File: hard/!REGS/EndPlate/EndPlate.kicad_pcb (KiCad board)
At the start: 2 copper layers, 68.6 x 61 mm, 10 parts, among them J1 Conn_01x13_Socket, J2 Conn_01x13_Socket, J3 Conn_01x13_Socket, J4 Conn_01x13_Socket, J5 Conn_01x13_Socket, J6 Conn_01x13_Socket, J7 Conn_01x13_Socket, J8 Conn_01x13_Socket, U1 74HC245, U2 74HC245

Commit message: End Plate PCB in work
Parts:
- added J10: Conn_01x03_Pin, Connector_PinHeader_2.54mm:PinHeader_1x03_P2.54mm_Vertical, F.Cu at (109.2, 43.2)
- added J9: Conn_01x03_Pin, Connector_PinHeader_2.54mm:PinHeader_1x03_P2.54mm_Vertical, F.Cu at (109.2, 53.3)
- J1, J2, J3, J4, J5, J6, J7, J8: footprint Connector_PinSocket_2.54mm:PinSocket_1x13_P2.54mm_Vertical -> Connector_PinSocket_2.54mm:PinSocket_1x13_P2.54mm_Vertical_SMD_Pin1Left
- moved J8 55.4 mm to (50.8, 40.6), turned to 180 degrees
- moved J1 55.4 mm to (104.1, 40.6), turned to 180 degrees
- moved J2 41.0 mm to (96.5, 40.6), turned to 180 degrees
- moved J7 41.0 mm to (58.4, 40.6), turned to 180 degrees
- moved J3 27.4 mm to (88.9, 40.6), turned to 180 degrees
- moved J6 27.4 mm to (66.0, 40.6), turned to 180 degrees
- moved U1 23.4 mm to (73.7, 68.6), turned to -90 degrees
- moved U2 23.4 mm to (104.1, 68.6), turned to -90 degrees
- moved J4 16.8 mm to (81.3, 40.6), turned to 180 degrees
- moved J5 16.8 mm to (73.7, 40.6), turned to 180 degrees
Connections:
- J1 pad 10: /S1.2 -> unconnected-(J1-Pin_10-Pad10)
- J1 pad 11: /~E1 -> /DST0
- J1 pad 6: /DST0 -> /S1.0
- J1 pad 7: unconnected-(J1-Pin_7-Pad7) -> /S1.1
- J1 pad 8: /S1.0 -> /S1.2
- J1 pad 9: /S1.1 -> /~E1
- J2 pad 10: /S1.2 -> unconnected-(J2-Pin_10-Pad10)
- J2 pad 11: /~E1 -> /DST1
- J2 pad 6: /DST1 -> /S1.0
- J2 pad 7: unconnected-(J2-Pin_7-Pad7) -> /S1.1
- J2 pad 8: /S1.0 -> /S1.2
- J2 pad 9: /S1.1 -> /~E1
- J3 pad 10: /S1.2 -> unconnected-(J3-Pin_10-Pad10)
- J3 pad 11: /~E1 -> /DST2
- J3 pad 6: /DST2 -> /S1.0
- J3 pad 7: unconnected-(J3-Pin_7-Pad7) -> /S1.1
- J3 pad 8: /S1.0 -> /S1.2
- J3 pad 9: /S1.1 -> /~E1
- J4 pad 10: /S1.2 -> unconnected-(J4-Pin_10-Pad10)
- J4 pad 11: /~E1 -> /DST3
- J4 pad 6: /DST3 -> /S1.0
- J4 pad 7: unconnected-(J4-Pin_7-Pad7) -> /S1.1
- J4 pad 8: /S1.0 -> /S1.2
- J4 pad 9: /S1.1 -> /~E1
- J5 pad 10: /S1.2 -> unconnected-(J5-Pin_10-Pad10)
- J5 pad 11: /~E1 -> /DST4
- J5 pad 6: /DST4 -> /S1.0
- J5 pad 7: unconnected-(J5-Pin_7-Pad7) -> /S1.1
- J5 pad 8: /S1.0 -> /S1.2
- J5 pad 9: /S1.1 -> /~E1
- J6 pad 10: /S1.2 -> unconnected-(J6-Pin_10-Pad10)
- J6 pad 11: /~E1 -> /DST5
- J6 pad 6: /DST5 -> /S1.0
- J6 pad 7: unconnected-(J6-Pin_7-Pad7) -> /S1.1
- J6 pad 8: /S1.0 -> /S1.2
- J6 pad 9: /S1.1 -> /~E1
- J7 pad 10: /S1.2 -> unconnected-(J7-Pin_10-Pad10)
- J7 pad 11: /~E1 -> /DST6
- J7 pad 6: /DST6 -> /S1.0
- J7 pad 7: unconnected-(J7-Pin_7-Pad7) -> /S1.1
- J7 pad 8: /S1.0 -> /S1.2
- J7 pad 9: /S1.1 -> /~E1
- J8 pad 10: /S1.2 -> unconnected-(J8-Pin_10-Pad10)
- J8 pad 11: /~E1 -> /DST7
- J8 pad 6: /DST7 -> /S1.0
- J8 pad 7: unconnected-(J8-Pin_7-Pad7) -> /S1.1
- J8 pad 8: /S1.0 -> /S1.2
- J8 pad 9: /S1.1 -> /~E1
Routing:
- net /S1.2: track 0.00 -> 60.1 mm
- net /S1.0: track 0.00 -> 60.1 mm
- net /S0.2: track 0.00 -> 60.1 mm
- net /S0.0: track 0.00 -> 60.1 mm
- net /S1.1: track 0.00 -> 56.8 mm
- net /S0.1: track 0.00 -> 56.8 mm
- net VCC: track 0.00 -> 53.3 mm
- net GND: track 0.00 -> 53.3 mm
- net /~E1: track 0.00 -> 53.3 mm
- net /~E0: track 0.00 -> 53.3 mm
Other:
- board text added: "The connectors are installed upside down because the multiplexer boards are installed upside down!"

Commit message: End Plate in work
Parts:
- added C1: 0,1uF, Capacitor_THT:C_Axial_L12.0mm_D6.5mm_P15.00mm_Horizontal, B.Cu at (82.5, 71.1)
- added C2: 0,1uF, Capacitor_THT:C_Axial_L12.0mm_D6.5mm_P15.00mm_Horizontal, B.Cu at (102.9, 71.2)
- added J11: Conn_01x09_Pin, Connector_PinHeader_2.54mm:PinHeader_1x09_P2.54mm_Vertical, F.Cu at (90.2, 67.3)
- added J12: Conn_01x09_Pin, Connector_PinHeader_2.54mm:PinHeader_1x09_P2.54mm_Vertical, F.Cu at (110.5, 67.3)
- added J13: Conn_01x09_Pin, Connector_PinHeader_2.54mm:PinHeader_1x09_P2.54mm_Vertical, F.Cu at (113.0, 67.3)
- added J14: Conn_01x09_Pin, Connector_PinHeader_2.54mm:PinHeader_1x09_P2.54mm_Vertical, F.Cu at (92.7, 67.3)
- added J15: Conn_01x01_Pin, Connector_PinHeader_2.54mm:PinHeader_1x01_P2.54mm_Vertical, F.Cu at (90.8, 61.6)
- added J16: Conn_01x01_Pin, Connector_PinHeader_2.54mm:PinHeader_1x01_P2.54mm_Vertical, F.Cu at (111.1, 61.6)
- added R1: 10k, Resistor_SMD:R_0805_2012Metric_Pad1.20x1.40mm_HandSolder, B.Cu at (82.5, 64.8)
- added R2: 10k, Resistor_SMD:R_0805_2012Metric_Pad1.20x1.40mm_HandSolder, B.Cu at (102.9, 64.8)
- added R3: 10k, Resistor_SMD:R_0805_2012Metric_Pad1.20x1.40mm_HandSolder, B.Cu at (91.7, 64.8)
- added R4: 10k, Resistor_SMD:R_0805_2012Metric_Pad1.20x1.40mm_HandSolder, B.Cu at (112.0, 64.8)
- J1, J2, J3, J4, J5, J6, J7, J8: moved to B.Cu
- moved J9 7.85 mm to (111.1, 45.7)
- moved J10 7.85 mm to (111.1, 35.6)
- moved U1 6.35 mm to (78.7, 64.8), turned to 0 degrees
- moved U2 6.35 mm to (99.1, 64.8), turned to 0 degrees
- turned J1 to 0 degrees
- turned J2 to 0 degrees
- turned J3 to 0 degrees
- turned J4 to 0 degrees
- turned J5 to 0 degrees
- turned J6 to 0 degrees
- turned J7 to 0 degrees
- turned J8 to 0 degrees
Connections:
- J1 pad 1: VCC -> /DST0
- J1 pad 10: unconnected-(J1-Pin_10-Pad10) -> /S1.1
- J1 pad 11: /DST0 -> /S1.2
- J1 pad 12: /SRC0 -> /~E1
- J1 pad 2: /S0.0 -> /SRC0
- J1 pad 3: /S0.1 -> unconnected-(J1-Pin_3-Pad3)
- J1 pad 4: /S0.2 -> VCC
- J1 pad 5: /~E0 -> /S0.0
- J1 pad 6: /S1.0 -> /S0.1
- J1 pad 7: /S1.1 -> /S0.2
- J1 pad 8: /S1.2 -> /~E0
- J1 pad 9: /~E1 -> /S1.0
- J2 pad 1: VCC -> /DST1
- J2 pad 10: unconnected-(J2-Pin_10-Pad10) -> /S1.1
- J2 pad 11: /DST1 -> /S1.2
- J2 pad 12: /SRC1 -> /~E1
- J2 pad 2: /S0.0 -> /SRC1
- J2 pad 3: /S0.1 -> unconnected-(J2-Pin_3-Pad3)
- J2 pad 4: /S0.2 -> VCC
- J2 pad 5: /~E0 -> /S0.0
- J2 pad 6: /S1.0 -> /S0.1
- J2 pad 7: /S1.1 -> /S0.2
- J2 pad 8: /S1.2 -> /~E0
- J2 pad 9: /~E1 -> /S1.0
- J3 pad 1: VCC -> /DST2
- J3 pad 10: unconnected-(J3-Pin_10-Pad10) -> /S1.1
- J3 pad 11: /DST2 -> /S1.2
- J3 pad 12: /SRC2 -> /~E1
- J3 pad 2: /S0.0 -> /SRC2
- J3 pad 3: /S0.1 -> unconnected-(J3-Pin_3-Pad3)
- J3 pad 4: /S0.2 -> VCC
- J3 pad 5: /~E0 -> /S0.0
- J3 pad 6: /S1.0 -> /S0.1
- J3 pad 7: /S1.1 -> /S0.2
- J3 pad 8: /S1.2 -> /~E0
- J3 pad 9: /~E1 -> /S1.0
- J4 pad 1: VCC -> /DST3
- J4 pad 10: unconnected-(J4-Pin_10-Pad10) -> /S1.1
- J4 pad 11: /DST3 -> /S1.2
- J4 pad 12: /SRC3 -> /~E1
- J4 pad 2: /S0.0 -> /SRC3
- J4 pad 3: /S0.1 -> unconnected-(J4-Pin_3-Pad3)
- J4 pad 4: /S0.2 -> VCC
- J4 pad 5: /~E0 -> /S0.0
- J4 pad 6: /S1.0 -> /S0.1
- J4 pad 7: /S1.1 -> /S0.2
- J4 pad 8: /S1.2 -> /~E0
- J4 pad 9: /~E1 -> /S1.0
- J5 pad 1: VCC -> /DST4
- J5 pad 10: unconnected-(J5-Pin_10-Pad10) -> /S1.1
- J5 pad 11: /DST4 -> /S1.2
- J5 pad 12: /SRC4 -> /~E1
- J5 pad 2: /S0.0 -> /SRC4
- J5 pad 3: /S0.1 -> unconnected-(J5-Pin_3-Pad3)
- J5 pad 4: /S0.2 -> VCC
- J5 pad 5: /~E0 -> /S0.0
- J5 pad 6: /S1.0 -> /S0.1
- J5 pad 7: /S1.1 -> /S0.2
- J5 pad 8: /S1.2 -> /~E0
- J5 pad 9: /~E1 -> /S1.0
- J6 pad 1: VCC -> /DST5
- J6 pad 10: unconnected-(J6-Pin_10-Pad10) -> /S1.1
- J6 pad 11: /DST5 -> /S1.2
- J6 pad 12: /SRC5 -> /~E1
- J6 pad 2: /S0.0 -> /SRC5
- J6 pad 3: /S0.1 -> unconnected-(J6-Pin_3-Pad3)
- J6 pad 4: /S0.2 -> VCC
- J6 pad 5: /~E0 -> /S0.0
- J6 pad 6: /S1.0 -> /S0.1
- J6 pad 7: /S1.1 -> /S0.2
- J6 pad 8: /S1.2 -> /~E0
- J6 pad 9: /~E1 -> /S1.0
- J7 pad 1: VCC -> /DST6
- J7 pad 10: unconnected-(J7-Pin_10-Pad10) -> /S1.1
- J7 pad 11: /DST6 -> /S1.2
- J7 pad 12: /SRC6 -> /~E1
- J7 pad 2: /S0.0 -> /SRC6
- J7 pad 3: /S0.1 -> unconnected-(J7-Pin_3-Pad3)
- J7 pad 4: /S0.2 -> VCC
- J7 pad 5: /~E0 -> /S0.0
- J7 pad 6: /S1.0 -> /S0.1
- J7 pad 7: /S1.1 -> /S0.2
- J7 pad 8: /S1.2 -> /~E0
- J7 pad 9: /~E1 -> /S1.0
- J8 pad 1: VCC -> /DST7
- J8 pad 10: unconnected-(J8-Pin_10-Pad10) -> /S1.1
- J8 pad 11: /DST7 -> /S1.2
- J8 pad 12: /SRC7 -> /~E1
- J8 pad 2: /S0.0 -> /SRC7
- J8 pad 3: /S0.1 -> unconnected-(J8-Pin_3-Pad3)
- J8 pad 4: /S0.2 -> VCC
- J8 pad 5: /~E0 -> /S0.0
- J8 pad 6: /S1.0 -> /S0.1
- J8 pad 7: /S1.1 -> /S0.2
- J8 pad 8: /S1.2 -> /~E0
- J8 pad 9: /~E1 -> /S1.0
- U1 pad 1: unconnected-(U1-A->B-Pad1) -> Net-(U1-A->B)
- U1 pad 19: unconnected-(U1-CE-Pad19) -> Net-(J15-Pin_1)
- U2 pad 1: unconnected-(U2-A->B-Pad1) -> Net-(U2-A->B)
- U2 pad 19: unconnected-(U2-CE-Pad19) -> Net-(J16-Pin_1)
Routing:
- net GND: track 53.3 -> 261.4 mm
- net /SRC7: track 0.00 -> 76.0 mm
- net /SRC6: track 0.00 -> 66.6 mm
- net /DST7: track 0.00 -> 57.7 mm
- net /SRC5: track 0.00 -> 56.4 mm
- net /SRC3: track 0.00 -> 53.6 mm
- net /SRC4: track 0.00 -> 53.2 mm
- net /DST6: track 0.00 -> 48.3 mm
- net /SRC2: track 0.00 -> 44.5 mm
- net VCC: track 53.3 -> 94.3 mm
- net /DST5: track 0.00 -> 38.5 mm
- net /DST0: track 0.00 -> 35.7 mm
- net /DST1: track 0.00 -> 33.6 mm
- net /DST4: track 0.00 -> 32.2 mm
- net /DST3: track 0.00 -> 31.3 mm
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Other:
- board size 68.6 x 61 mm -> 74.9 x 68.6 mm
- board text added: "DST"
- board text added: "Gnd"
- board text added: "SRC"

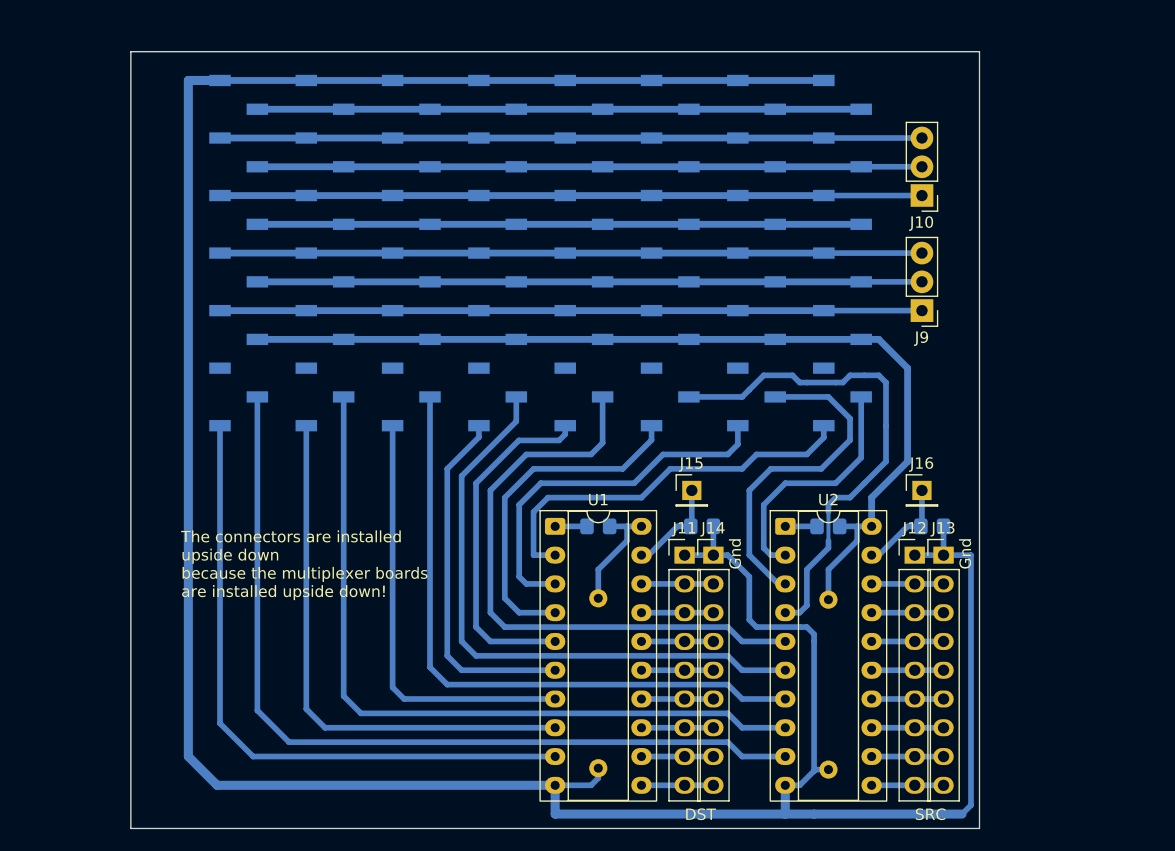
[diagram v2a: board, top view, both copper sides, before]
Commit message: End Plate polishing
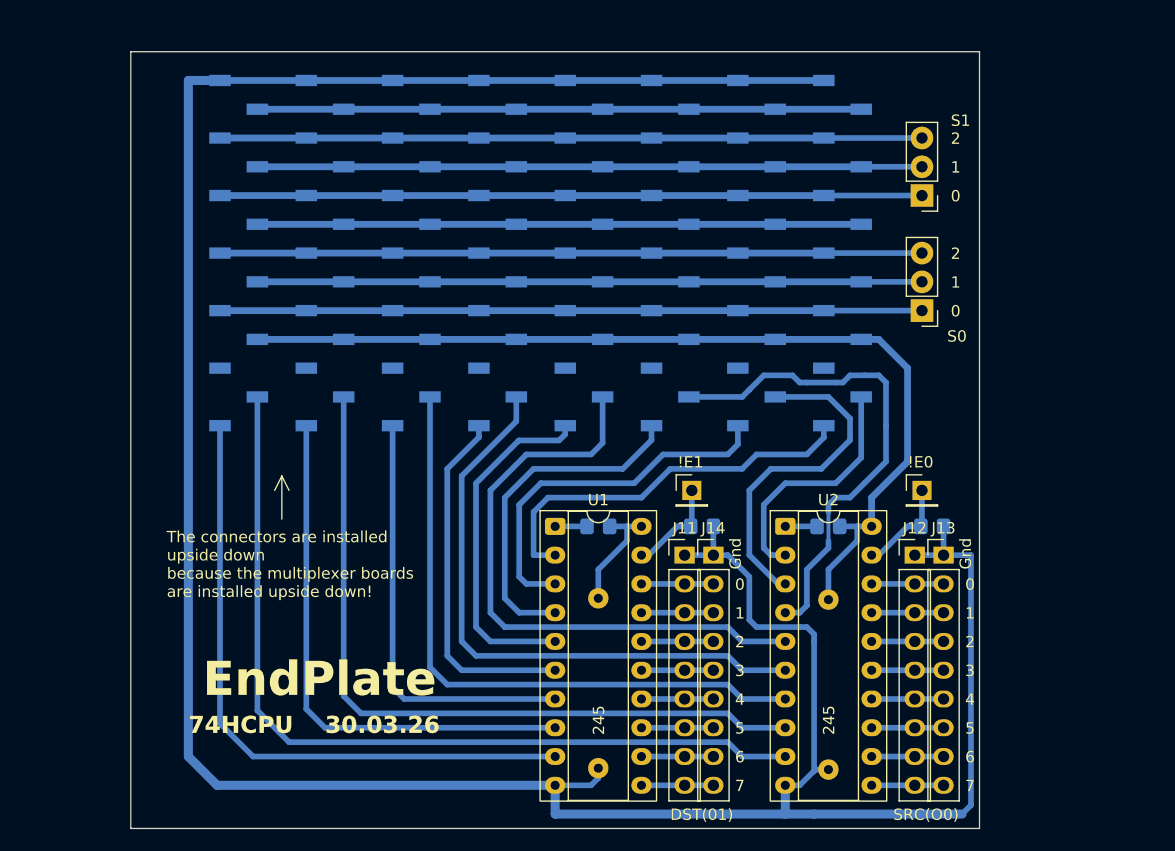
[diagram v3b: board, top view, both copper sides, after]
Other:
- board text added: "!E0"
- board text added: "!E1"
- board text added: "0"
- board text added: "1"
- board text added: "2"
- board text added: "245"
- board text added: "3"
- board text added: "30.03.26"
- board text added: "4"
- board text added: "5"
- board text added: "6"
- board text added: "7"
- board text added: "74HCPU"
- board text added: "DST(01)"
- board text added: "EndPlate"
- board text added: "S0"
- board text added: "S1"
- board text added: "SRC(O0)"
- board text removed: "DST"
- board text removed: "SRC"

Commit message: Move gerbers to subfolder
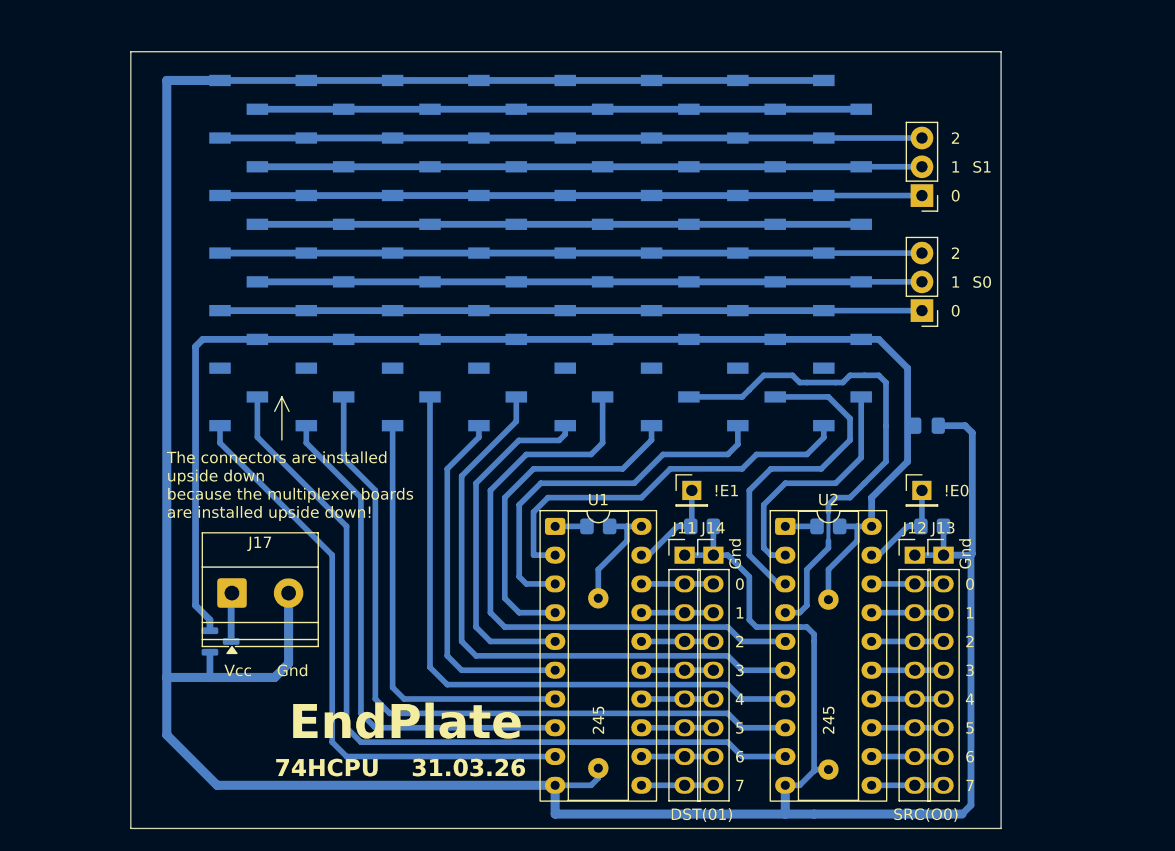
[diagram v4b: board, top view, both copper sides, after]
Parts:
- added C3: 0,1uF, Capacitor_SMD:C_0805_2012Metric_Pad1.18x1.45mm_HandSolder, B.Cu at (111.5, 55.9)
- added J17: Screw_Terminal_01x02, TerminalBlock_Phoenix:TerminalBlock_Phoenix_MKDS-1,5-2_1x02_P5.00mm_Horizontal, F.Cu at (50.2, 70.7)
- added Q1: IRLML5203, Package_TO_SOT_SMD:SOT-23, B.Cu at (49.2, 74.9)
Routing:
- net GND: track 261.4 -> 297.9 mm
- net VCC: track 94.3 -> 125.7 mm
- net /DST7: track 57.7 -> 52.9 mm
- net Net-(J17-Pin_1): track 0.00 -> 4.30 mm
- net /SRC7: track 76.0 -> 72.3 mm
- net /DST6: track 48.3 -> 45.7 mm
- net /SRC6: track 66.6 -> 65.1 mm
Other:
- board size 74.9 x 68.6 mm -> 76.8 x 68.6 mm
- board text added: "31.03.26"
- board text added: "DSTx"
- board text added: "NC"
- board text added: "S0.0"
- board text added: "S0.1"
- board text added: "S0.2"
- board text added: "S1.0"
- board text added: "S1.1"
- board text added: "S1.2"
- board text added: "SRCx"
- board text added: "Vcc"
- board text removed: "30.03.26"

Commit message: End Plate polishing
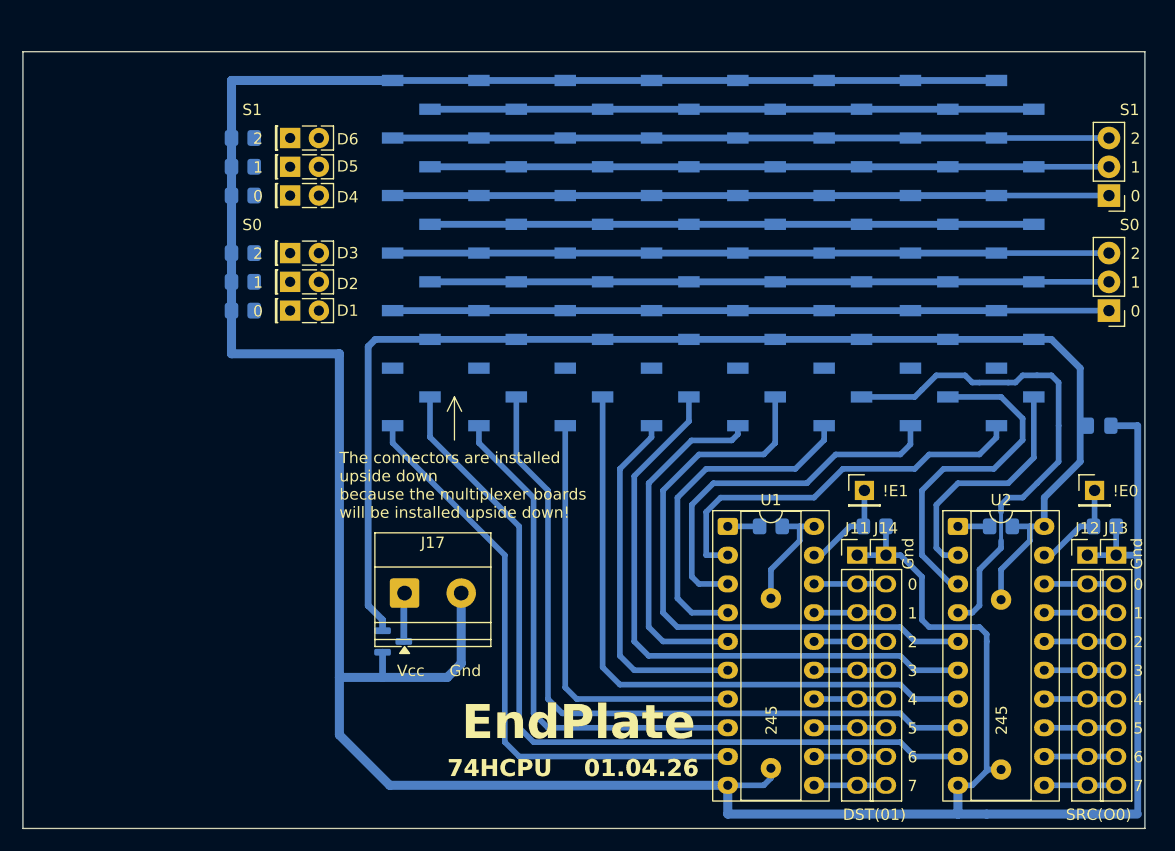
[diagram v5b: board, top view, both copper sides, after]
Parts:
- added D1: LED, LED_THT:LED_Rectangular_W5.0mm_H2.0mm, F.Cu at (55.3, 45.7)
- added D2: LED, LED_THT:LED_Rectangular_W5.0mm_H2.0mm, F.Cu at (55.3, 43.2)
- added D3: LED, LED_THT:LED_Rectangular_W5.0mm_H2.0mm, F.Cu at (55.3, 40.6)
- added D4: LED, LED_THT:LED_Rectangular_W5.0mm_H2.0mm, F.Cu at (55.3, 35.6)
- added D5: LED, LED_THT:LED_Rectangular_W5.0mm_H2.0mm, F.Cu at (55.3, 33.0)
- added D6: LED, LED_THT:LED_Rectangular_W5.0mm_H2.0mm, F.Cu at (55.3, 30.5)
- added R10: 1k, Resistor_SMD:R_0805_2012Metric_Pad1.20x1.40mm_HandSolder, B.Cu at (51.2, 30.5)
- added R5: 1k, Resistor_SMD:R_0805_2012Metric_Pad1.20x1.40mm_HandSolder, B.Cu at (51.2, 45.7)
- added R6: 1k, Resistor_SMD:R_0805_2012Metric_Pad1.20x1.40mm_HandSolder, B.Cu at (51.2, 43.2)
- added R7: 1k, Resistor_SMD:R_0805_2012Metric_Pad1.20x1.40mm_HandSolder, B.Cu at (51.2, 40.6)
- added R8: 1k, Resistor_SMD:R_0805_2012Metric_Pad1.20x1.40mm_HandSolder, B.Cu at (51.2, 35.6)
- added R9: 1k, Resistor_SMD:R_0805_2012Metric_Pad1.20x1.40mm_HandSolder, B.Cu at (51.2, 33.0)
- moved J10 16.5 mm to (127.6, 35.6)
- moved J9 16.5 mm to (127.6, 45.7)
- moved C1 15.2 mm to (97.8, 71.1)
- moved J12 15.2 mm to (125.7, 67.3)
- moved J13 15.2 mm to (128.3, 67.3)
- moved J14 15.2 mm to (108.0, 67.3)
- moved J2 15.2 mm to (111.8, 40.6)
- moved J5 15.2 mm to (88.9, 40.6)
- moved J8 15.2 mm to (66.0, 40.6)
- moved R1 15.2 mm to (97.8, 64.8)
- moved R3 15.2 mm to (107.0, 64.8)
- moved U1 15.2 mm to (94.0, 64.8)
- moved Q1 15.2 mm to (64.4, 74.9)
- moved C2 15.2 mm to (118.1, 71.2)
- moved C3 15.2 mm to (126.8, 55.9)
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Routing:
- net GND: track 297.9 -> 316.1 mm
- net /S1.1: track 58.7 -> 59.9 mm
- net /S0.1: track 58.7 -> 59.9 mm
- net /S1.0: track 62.0 -> 63.2 mm
- net /S0.2: track 62.0 -> 63.2 mm
- net /S1.2: track 62.0 -> 63.2 mm
- net /S0.0: track 62.0 -> 63.2 mm
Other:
- board size 76.8 x 68.6 mm -> 99.1 x 68.6 mm
- board text added: "01.04.26"
- board text added: "The connectors are installed upside down because the multiplexer boards will be installed upside down!"
- board text removed: "31.03.26"
- board text removed: "The connectors are installed upside down because the multiplexer boards are installed upside down!"

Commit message: EndPlate pcb polishing
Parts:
- moved C1 3.81 mm to (94.0, 71.1)
- moved J11 3.81 mm to (101.6, 67.3)
- moved J14 3.81 mm to (104.1, 67.3)
- moved J15 3.81 mm to (102.2, 61.6)
- moved R1 3.81 mm to (94.0, 64.8)
- moved R3 3.81 mm to (103.1, 64.8)
- moved U1 3.81 mm to (90.2, 64.8)
- moved J13 1.91 mm to (126.4, 67.3)
- moved C2 1.91 mm to (116.2, 71.2)
- moved J12 1.91 mm to (123.8, 67.3)
- moved J16 1.91 mm to (124.5, 61.6)
- moved R2 1.91 mm to (116.2, 64.8)
- moved R4 1.91 mm to (125.4, 64.8)
- moved U2 1.91 mm to (112.4, 64.8)
- moved C3 0.47 mm to (127.2, 55.9)
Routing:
- net VCC: track 125.7 -> 144.5 mm, vias 0 -> 2
- net /DST0: track 35.7 -> 46.2 mm
- net /S1.1: track 59.9 -> 69.8 mm
- net /S0.1: track 59.9 -> 69.8 mm
- net /S1.2: track 63.2 -> 69.8 mm
- net /S0.0: track 63.2 -> 69.8 mm
- net /S1.0: track 63.2 -> 69.8 mm
- net /S0.2: track 63.2 -> 69.8 mm
- net /SRC4: track 53.2 -> 58.9 mm
- net /SRC3: track 53.6 -> 58.7 mm
- net /SRC5: track 56.4 -> 60.0 mm
- net /DST7: track 52.9 -> 49.6 mm
- net /DST6: track 45.7 -> 42.4 mm
- net GND: track 316.1 -> 312.9 mm
- net Net-(D6-K): track 0.00 -> 3.18 mm
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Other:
- board text added: "17.04.26"
- board text removed: "01.04.26"
